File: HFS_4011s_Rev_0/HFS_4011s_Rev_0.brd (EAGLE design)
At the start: 44.5 x 47 mm, 64 parts, among them IC1 CP2104, J1 2X06, J2 2X12, J3 1X02, J5 1X02, J6 MOLEX_IGRID_15X2CONNECTOR, Q1 mmbt2222, Q2 mmbt2222, Q3 MMUN2133LT1G, Q4 BSS138, Q5 BSS138, SW2 KMR2, U1 TPS61090RSAR, U2 MCP73831T-2ACI/OT, U3 AD5693R, U4 LM3671MF-3.3/NOPB, X2 ESP32_WROOM32_SKINNY

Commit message: Started board layout. Placed battery charge circuitry, usb-serial conversion, and reset components onto board.
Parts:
- removed R13: 10K, microbuilder:RESPACK_4X0603
- added C15: 4.7uF, rcl:C1206
- added R24, R25, R26: 10k, rcl:R0603
- C2: device microbuilder:0805-NO -> rcl:C0603
- moved R16 244.1 mm to (14.5, 7.37), flipped to the bottom, turned to 90 degrees
- moved R15 235.1 mm to (14.5, 3.30), flipped to the bottom, turned to 90 degrees
- moved Q3 214.7 mm to (-0.95, -295.8)
- moved C7 98.8 mm to (4.06, 11.7)
- moved U1 95.1 mm to (10.2, 8.64)
- moved L1 81.4 mm to (4.32, 4.06)
- moved R8 66.9 mm to (36.8, 20.6)
- moved LED3 65.5 mm to (33.3, 27.4)
- moved LED4 65.0 mm to (36.3, 27.4)
- moved C6 64.9 mm to (33.3, 23.4), turned to 270 degrees
- moved U2 64.1 mm to (36.8, 23.6), turned to 90 degrees
- moved R6 63.6 mm to (33.3, 31.0), turned to 90 degrees
- moved R7 62.3 mm to (36.8, 30.5), turned to 180 degrees
- moved SW2 34.4 mm to (35.3, 1.78), turned to 180 degrees
- moved Q1 30.8 mm to (34.5, 2.29), flipped to the bottom
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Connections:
- new net SHLD: J4.SHLD1, J4.SHLD2, J4.SHLD3, J4.SHLD4, J4.SHLD5, J4.SHLD6, J4.SHLD7, J4.SHLD8
- net 3.3V: now also R26.2; no longer R13.3
- net 5.0V: now also J5.2
- net DTR: now also R25.1; no longer R13.4
- net GND: now also C15.2; no longer J5.2
- net N$12: now also R25.2; no longer R13.5
- net N$13: now also R24.2; no longer R13.2
- net RESET: now also R26.1; no longer R13.6
- net RTS: now also R24.1; no longer R13.7
- net VBAT: now also C15.1
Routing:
- net VBUS: track 0.00 -> 45.7 mm, vias 0 -> 3
- net N$6: track 0.00 -> 24.0 mm, vias 0 -> 2
- net RESET: track 0.00 -> 23.4 mm, vias 0 -> 1
- net N$2: track 0.00 -> 22.2 mm, vias 0 -> 2
- net GPIO0: track 0.00 -> 17.8 mm
- net RTS: track 0.00 -> 15.8 mm, vias 0 -> 1
- net N$7: track 0.00 -> 13.3 mm
- net DTR: track 0.00 -> 11.9 mm, vias 0 -> 1
- net 3.3V: track 0.00 -> 11.4 mm, vias 0 -> 2
- net N$18: track 0.00 -> 11.1 mm, vias 0 -> 1
- net N$19: track 0.00 -> 10.9 mm, vias 0 -> 1
- net N$16: track 0.00 -> 7.56 mm
- net N$9: track 0.00 -> 4.58 mm
- net N$12: track 0.00 -> 3.50 mm
- net N$13: track 0.00 -> 3.34 mm, vias 0 -> 1
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- added copper zone on layer 1, net SHLD
- added copper zone on layer 16, net SHLD
- added copper zone on layer 1, net VBAT

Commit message: Changed usb C back to micro usb. Converted board to a 4-layer design. Routed 5V power supply.
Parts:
- removed R1, R3: 100K, microbuilder:0603-NO
- removed R15, R16: 5.1k, rcl:R0603
- C1, C10, C11, C3, C5, C6: device microbuilder:0805-NO -> rcl:C0603
- C4: device microbuilder:0603-NO -> rcl:C0603
- J4: value (none) -> microUSB; device SparkFun-Connectors:USB-C-16P -> microbuilder:4UCONN_20329
- R10: device microbuilder:0603-NO -> rcl:R0603
- R11, R12, R14, R2, R20, R4, R5, R6, R7, R8, R9: device microbuilder:0805-NO -> rcl:R0603
- R18: value (none) -> 5k
- moved Q3 307.5 mm to (15.8, 11.2), flipped to the bottom, turned to 90 degrees
- moved D1 141.0 mm to (4.32, 6.10), flipped to the bottom
- moved R9 117.2 mm to (11.2, 12.7), flipped to the bottom
- moved C3 113.3 mm to (4.32, 8.64), turned to 180 degrees
- moved R4 112.3 mm to (10.9, 13.0), turned to 180 degrees
- moved R5 108.9 mm to (17.5, 8.13)
- moved R20 108.0 mm to (16.5, 8.64), flipped to the bottom, turned to 180 degrees
- moved C1 107.7 mm to (5.59, 3.56), flipped to the bottom
- moved PWR 107.6 mm to (15.7, 2.03)
- moved LBO 107.1 mm to (13.7, 2.03), turned to 180 degrees
- moved C5 106.9 mm to (5.59, 1.52), flipped to the bottom
- moved R11 106.0 mm to (14.2, 6.86), turned to 180 degrees
- moved R2 105.1 mm to (13.0, 4.57), flipped to the bottom, turned to 180 degrees
- moved R12 103.9 mm to (13.0, 4.83), turned to 180 degrees
- moved C4 21.7 mm to (36.3, 15.7), turned to 180 degrees
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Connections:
- removed net A0_DAC2: X2.11
- removed net A13_I35: R1.1, R3.2, X2.7
- removed net A1_DAC1: X2.10
- removed net A2_I34: X2.6
- removed net A3_I39: X2.5
- removed net A4_IO36: X2.4
- removed net A5_IO4: X2.26
- removed net GPIO2: X2.24
- removed net IO12_A11: X2.14
- removed net IO14_A6: X2.13
- removed net IO15_A8: X2.23
- removed net IO16: X2.27
- removed net IO17: X2.28
- removed net IO21: X2.33
- removed net IO27_A10: X2.12
- removed net IO32_A7: X2.8
- removed net IO33_A9: X2.9
- removed net N$18: J4.A5, R16.2
- removed net N$19: J4.B5, R15.2
- removed net N$27: J2.14
- removed net N$28: J2.16
- removed net N$29: J2.18
- removed net N$39: J2.13
- removed net N$40: J2.15
- removed net N$41: J2.17
- removed net PB1_L: J6.P$12
- removed net PB2_L: J6.P$14
- removed net S0: J2.8
- removed net S2: J2.4
- removed net S6: J2.7
- removed net S7: J2.5
- removed net S8: J2.3
- removed net S9: J2.1
- removed net SHLD: J4.SHLD1, J4.SHLD2, J4.SHLD3, J4.SHLD4, J4.SHLD5, J4.SHLD6, J4.SHLD7, J4.SHLD8
- new net ANC_SW_H: J6.P$23, X2.13
- new net ANC_SW_OUT: J2.7, X2.14
- net 5.0V: no longer J6.P$23
- net DAC_OUT: now also J2.1
- net GND: now also J2.13, J2.14, J2.15, J2.16, J2.17, J2.18, J4.BASE@1, J4.BASE@2, J4.SPRT@1, J4.SPRT@2, J4.SPRT@3, J4.SPRT@4, J6.P$12, J6.P$14; no longer J4.GND2, R15.1, R16.1, R3.1
- net MIC1_AUD: now also J2.3
- net MIC2_AUD: now also J2.5
- net N$2: now also J4.D+; no longer J4.A6, J4.B6
- net N$6: now also J4.D-; no longer J4.A7, J4.B7
- net PB1_H: now also X2.27
- net PB2_H: now also X2.28
- net S1: no longer J2.6
- net S3: no longer J2.2
- net SPKR_L_N: now also J2.4
- net SPKR_L_P: now also J2.2
- net SPKR_R_N: now also J2.8
- net SPKR_R_P: now also J2.6
- net VBAT: no longer R1.2
- net VBUS: now also J4.VBUS; no longer J4.VBUS1, J4.VBUS2
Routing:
- net VBAT: track 0.00 -> 47.5 mm, vias 0 -> 2
- net 5.0V: track 0.00 -> 44.1 mm, vias 0 -> 3
- net GND: track 2.31 -> 42.8 mm, vias 1 -> 16
- net N$18: track 11.1 -> 0.00 mm, vias 1 -> 0
- net N$19: track 10.9 -> 0.00 mm, vias 1 -> 0
- net N$6: track 24.0 -> 16.6 mm
- net N$2: track 22.2 -> 15.8 mm
- net N$14: track 0.00 -> 6.36 mm, vias 0 -> 1
- net VBUS: track 45.7 -> 39.5 mm
- net ENABLE: track 0.00 -> 5.96 mm, vias 0 -> 1
- net N$10: track 0.00 -> 5.68 mm
- net RESET: track 23.4 -> 27.2 mm
- net N$4: track 0.00 -> 3.47 mm
- net N$11: track 0.00 -> 2.75 mm
- net N$15: track 0.00 -> 2.75 mm
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- added copper zone on layer 1, net 5.0V
- added copper zone on layer 2, net GND
- added copper zone on layer 1, net N$3
- added copper zone on layer 16, net VBAT
- removed copper zone on layer 1, net SHLD
- removed copper zone on layer 16, net SHLD

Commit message: Moved esp32 board up a little and added debug LED.
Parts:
- moved C14 217.8 mm to (55.9, -7.11)
- moved C8 217.8 mm to (55.9, 10.7)
- moved R17 217.8 mm to (54.6, -13.5)
- moved C12 217.8 mm to (55.9, 3.05)
- moved C13 217.8 mm to (55.9, -0.76)
- moved C9 217.8 mm to (55.9, 6.86)
- moved R18 217.8 mm to (54.6, -18.5)
- moved U3 217.8 mm to (55.9, 17.0)
- moved C10 208.5 mm to (30.5, 38.6), flipped to the bottom, turned to 270 degrees
- moved R14 207.6 mm to (21.3, 38.1), flipped to the bottom
- moved C11 206.1 mm to (14.0, 38.4), flipped to the bottom, turned to 90 degrees
- moved L2 201.3 mm to (17.8, 38.6), flipped to the bottom
- moved U4 201.1 mm to (26.7, 38.4), flipped to the bottom
- moved D3 31.7 mm to (18.5, 10.9), turned to 180 degrees
- moved R10 26.8 mm to (16.5, 11.2), turned to 270 degrees
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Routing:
- net 3.3V: track 12.1 -> 0.48 mm, vias 2 -> 0
- net VBAT: track 47.5 -> 58.3 mm, vias 2 -> 3
- net GND: track 42.8 -> 51.2 mm, vias 16 -> 19
- net N$5: track 0.00 -> 2.71 mm
- net IO13_A12: track 0.00 -> 2.28 mm
- net GPIO0: track 18.6 -> 20.4 mm

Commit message: All components on board. Need to finish routing some signals to connectors.
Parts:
- moved R23 303.9 mm to (22.9, 19.6), flipped to the bottom
- moved R22 301.3 mm to (31.5, 20.8), flipped to the bottom, turned to 90 degrees
- moved Q5 295.8 mm to (28.2, 20.8), flipped to the bottom, turned to 270 degrees
- moved R21 283.8 mm to (24.9, 14.2), flipped to the bottom, turned to 90 degrees
- moved R19 282.0 mm to (31.5, 16.5), flipped to the bottom, turned to 90 degrees
- moved Q4 276.5 mm to (28.2, 16.5), flipped to the bottom, turned to 270 degrees
- moved C14 61.3 mm to (16.5, 39.9), flipped to the bottom, turned to 180 degrees
- moved R18 55.9 mm to (23.9, 28.2), flipped to the bottom, turned to 270 degrees
- moved C12 54.9 mm to (12.2, 36.3), flipped to the bottom, turned to 270 degrees
- moved R17 53.2 mm to (21.6, 28.2), flipped to the bottom, turned to 270 degrees
- moved C13 51.9 mm to (16.5, 33.0), flipped to the bottom, turned to 180 degrees
- moved C9 46.8 mm to (21.1, 38.1), flipped to the bottom, turned to 270 degrees
- moved U3 43.8 mm to (16.5, 36.3), flipped to the bottom, turned to 270 degrees
- moved C8 42.2 mm to (21.1, 34.5), flipped to the bottom, turned to 90 degrees
- moved C10 25.9 mm to (13.0, 19.6)
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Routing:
- net 3.3V: track 0.48 -> 87.9 mm, vias 0 -> 5
- net SCL: track 0.00 -> 22.6 mm, vias 0 -> 2
- net SDA: track 0.00 -> 22.0 mm, vias 0 -> 2
- net 5.0V: track 44.1 -> 61.2 mm, vias 3 -> 4
- net GND: track 51.2 -> 66.9 mm, vias 19 -> 23
- net VBAT: track 58.3 -> 70.7 mm
- net SCK: track 0.00 -> 8.46 mm, vias 0 -> 1
- net DAC_OUT: track 0.00 -> 7.61 mm
- net MOSI: track 0.00 -> 6.16 mm, vias 0 -> 1
- net SCK_5V: track 0.00 -> 4.05 mm
- net MOSI_5V: track 0.00 -> 3.91 mm
- net EN: track 0.00 -> 2.41 mm
- net N$20: track 0.00 -> 2.35 mm
- net DTR: track 12.4 -> 10.6 mm
- added copper zone on layer 16, net 3.3V
- added copper zone on layer 16, net N$17

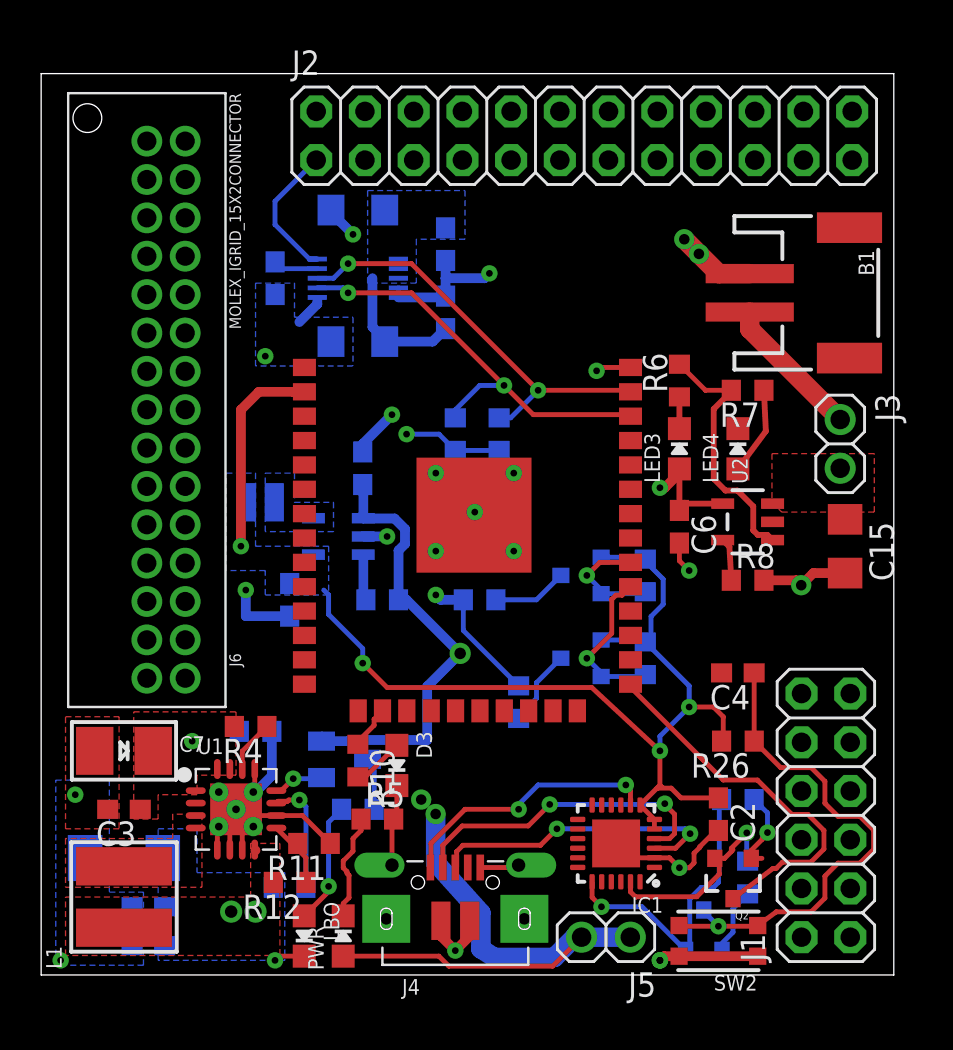
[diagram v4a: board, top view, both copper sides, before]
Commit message: Routed all components (0 airwire errors). But getting a lot of clearance errors. Also changed connector pinout
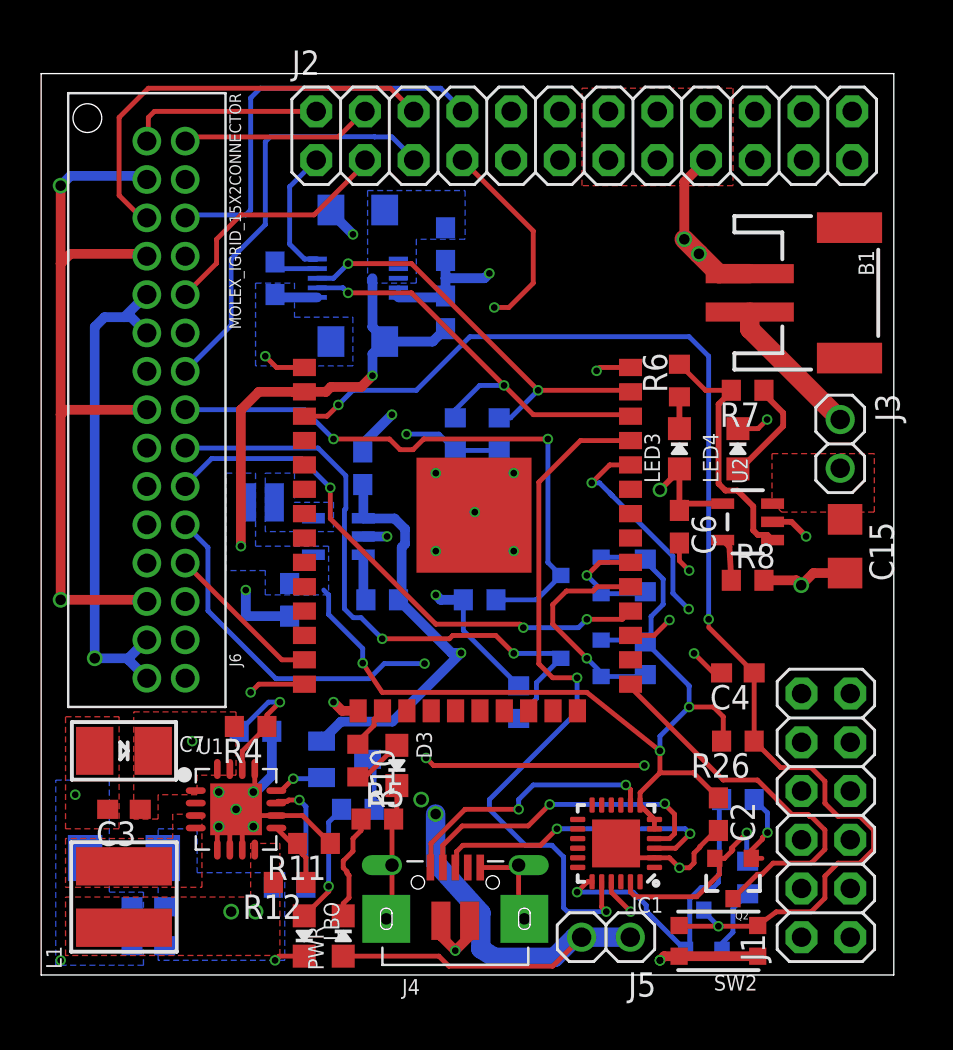
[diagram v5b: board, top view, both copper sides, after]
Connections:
- removed net S1: J1.8
- removed net S3: J1.10
- net 3.3V: now also J6.P$10, J6.P$12, J6.P$28, J6.P$30; no longer J6.P$27, J6.P$29, J6.P$5, J6.P$8
- net 5.0V: now also J6.P$16, J6.P$26, J6.P$4, J6.P$8; no longer J6.P$1, J6.P$15, J6.P$19, J6.P$25
- net GND: now also J6.P$11, J6.P$18, J6.P$22, J6.P$25, J6.P$27, J6.P$29, J6.P$3, J6.P$7; no longer J6.P$12, J6.P$16, J6.P$2, J6.P$26, J6.P$28, J6.P$30, J6.P$6, J6.P$9
- net MIC1_AUD: now also J6.P$9; no longer J6.P$7
- net MIC2_AUD: now also J6.P$13; no longer J6.P$10
- net MOSI_5V: now also J6.P$15; no longer J6.P$4
- net PB1_H: now also J6.P$21; no longer J6.P$11
- net PB2_H: now also J6.P$19; no longer J6.P$13
- net S5: no longer J1.12
- net SCK_5V: now also J6.P$17; no longer J6.P$3
- net SPKR_L_N: now also J6.P$1; no longer J6.P$18
- net SPKR_L_P: now also J6.P$2; no longer J6.P$17
- net SPKR_R_N: now also J6.P$5; no longer J6.P$22
- net SPKR_R_P: now also J6.P$6; no longer J6.P$21
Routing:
- net 5.0V: track 61.2 -> 117.3 mm, vias 4 -> 6
- net 3.3V: track 87.9 -> 139.5 mm, vias 5 -> 7
- net PB1_H: track 0.00 -> 45.1 mm, vias 0 -> 4
- net GND: track 66.9 -> 109.7 mm, vias 23 -> 27
- net RESET: track 27.2 -> 67.9 mm, vias 1 -> 3
- net ANC_SW_OUT: track 0.00 -> 39.7 mm, vias 0 -> 2
- net TXD0: track 0.00 -> 37.7 mm, vias 0 -> 2
- net RXD0: track 0.00 -> 31.3 mm, vias 0 -> 3
- net PB2_H: track 0.00 -> 28.8 mm, vias 0 -> 3
- net SCK_5V: track 4.05 -> 32.5 mm, vias 0 -> 2
- net MOSI_5V: track 3.91 -> 31.3 mm, vias 0 -> 2
- net SPKR_R_P: track 0.00 -> 22.5 mm
- net MIC2_AUD: track 0.00 -> 22.1 mm
- net SPKR_R_N: track 0.00 -> 21.2 mm
- net MIC1_AUD: track 0.00 -> 13.1 mm
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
